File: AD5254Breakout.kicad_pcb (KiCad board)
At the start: 2 copper layers, 20.6 x 18 mm, 13 parts, among them J1 Conn_01x08, J2 Conn_01x08, U1 AD5254

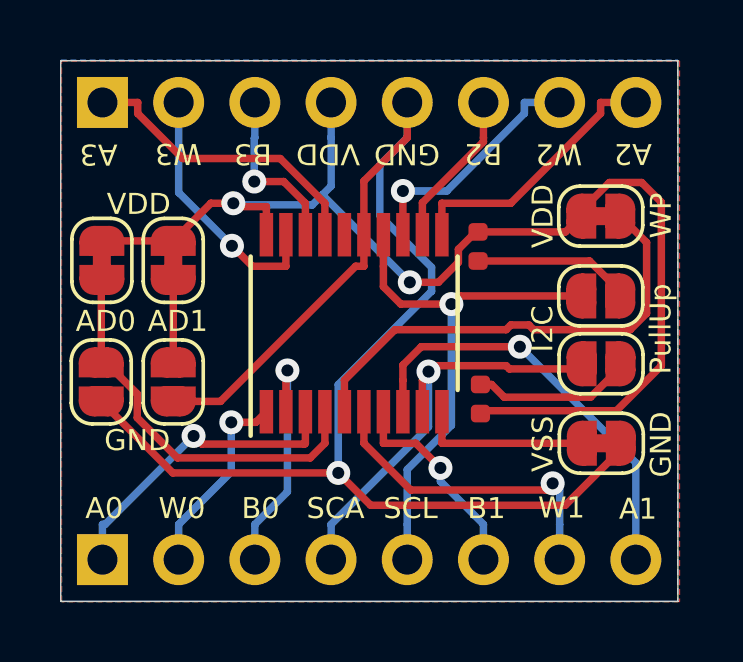
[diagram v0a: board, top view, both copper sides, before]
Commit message: Add missing A1 line to pcb
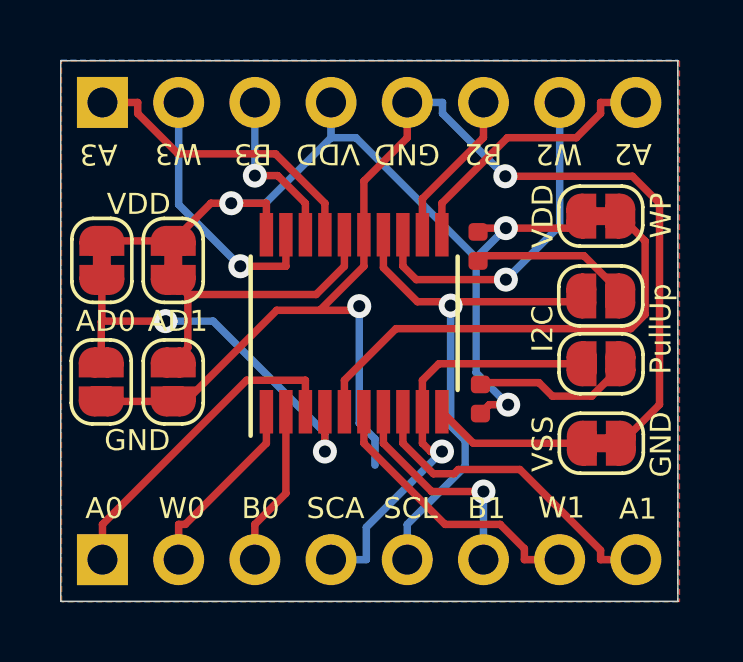
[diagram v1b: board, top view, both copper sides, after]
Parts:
- R1, R2: value R -> 10k
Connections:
- U1 pad 16: Net-(U1-Pad16) -> /AD1
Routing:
- net VDD: track 40.0 -> 30.4 mm, vias 2 -> 3
- net /AD1: track 2.75 -> 9.81 mm
- net GND: track 48.7 -> 42.1 mm, vias 1 -> 2
- net /A1: track 14.4 -> 10.7 mm, vias 1 -> 0
- net /W2: track 8.12 -> 11.3 mm
- net /B0: track 8.15 -> 5.36 mm, vias 1 -> 0
- net /W1: track 10.7 -> 9.40 mm, vias 1 -> 0
- net /A0: track 10.3 -> 11.0 mm, vias 1 -> 0
- net /VSS: track 5.72 -> 5.10 mm
- net /AD0: track 13.2 -> 13.7 mm, vias 0 -> 2
- net /W0: track 6.62 -> 6.27 mm, vias 1 -> 0
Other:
- board text added: "Rev2019.11"
- board text removed: "Rev2019.10"
